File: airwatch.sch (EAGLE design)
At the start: 34 parts, among them IC1 MCP1825 (3.3 or 3v), IC2 TP4056, J1 POWER_JACK, Q1 NCV4274, U1 ESP8266-01/ESP-01, U2 ADS1015IDGSR

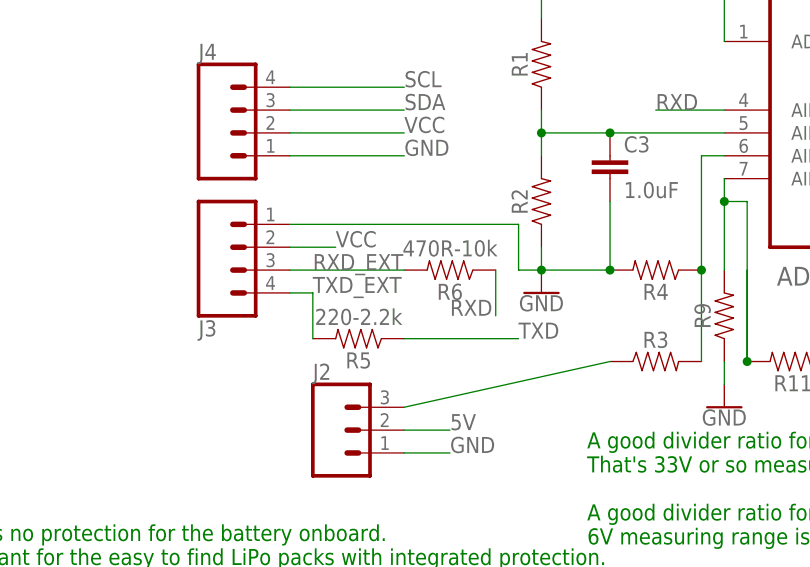
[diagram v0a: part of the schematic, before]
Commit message: Soldermask for the 0805-ez pads. Totally untested, might even revert.
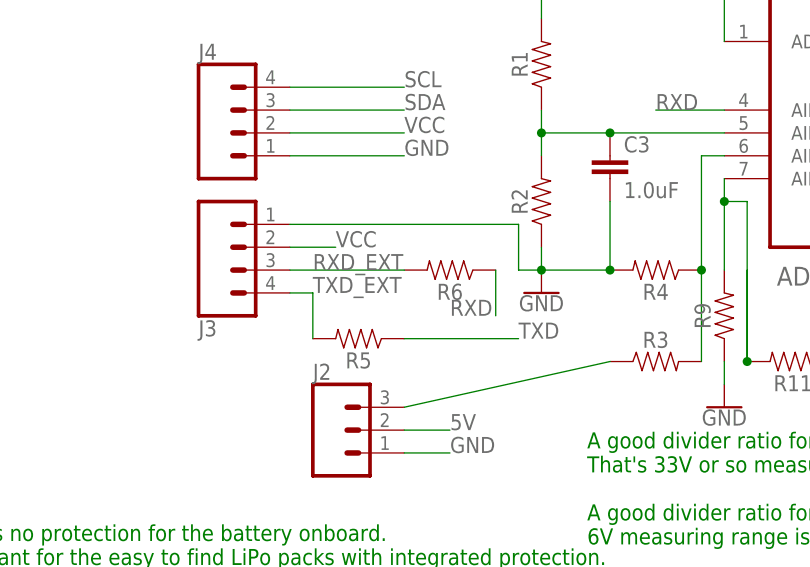
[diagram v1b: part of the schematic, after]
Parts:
- R5: value 220-2.2k -> (none)
- R6: value 470R-10k -> (none)
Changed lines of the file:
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@@
 <part name="C1" library="SparkFun-Capacitors" deviceset="10UF" device="-0805-10V-10%" value="10uF"/>
 <part name="GND2" library="SparkFun-PowerSymbols" deviceset="GND" device=""/>
-<part name="IC1" library="linear" deviceset="MCP1703" device="DB" value="MCP1825 (3.3 or 3v)"/>
+<part name="IC1" library="linear" library_urn="urn:adsk.eagle:library:262" deviceset="MCP1703" device="DB" package3d_urn="urn:adsk.eagle:package:16418/2" value="MCP1825 (3.3 or 3v)"/>
 <part name="C2" library="SparkFun-Capacitors" deviceset="10UF" device="-0805-10V-10%" value="10uF"/>
 <part name="GND3" library="SparkFun-PowerSymbols" deviceset="GND" device=""/>
@@
 <part name="R4" library="smd_passives_easy" deviceset="RESISTOR" device="0805" value=" "/>
 <part name="J3" library="SparkFun-Connectors" deviceset="CONN_04" device="JST-PTH-VERT"/>
-<part name="R5" library="smd_passives_easy" deviceset="RESISTOR" device="0805" value="220-2.2k"/>
+<part name="R5" library="smd_passives_easy" deviceset="RESISTOR" device="0805" value=" "/>
 <part name="J4" library="SparkFun-Connectors" deviceset="CONN_04" device="JST-PTH-VERT"/>
-<part name="R6" library="smd_passives_easy" deviceset="RESISTOR" device="0805" value="470R-10k"/>
+<part name="R6" library="smd_passives_easy" deviceset="RESISTOR" device="0805" value=" "/>
 <part name="GND7" library="SparkFun-PowerSymbols" deviceset="GND" device=""/>
 <part name="GND9" library="SparkFun-PowerSymbols" deviceset="GND" device=""/>
@@
 which will not be processed correctly with this version.
 </note>
+<note version="8.2" severity="warning">
+Since Version 8.2, EAGLE supports online libraries. The ids
+of those online libraries will not be understood (or retained)
+with this version.
+</note>
+<note version="8.3" severity="warning">
+Since Version 8.3, EAGLE supports URNs for individual library
+assets (packages, symbols, and devices). The URNs of those assets
+will not be understood (or retained) with this version.
+</note>
+<note version="8.3" severity="warning">
+Since Version 8.3, EAGLE supports the association of 3D packages
+with devices in libraries, schematics, and board files. Those 3D
+packages will not be understood (or retained) with this version.
+</note>
 </compatibility>
